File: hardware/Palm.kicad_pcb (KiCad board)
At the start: 2 copper layers, 29.8 x 70.5 mm, 13 parts, among them J1 Conn_01x02_Female, Q1 IRLML6402, SW1 SW_SPDT, SW2 SW_SPDT, U1 Adafruit_nRF52_Feather, U2 VEML6075_breakout

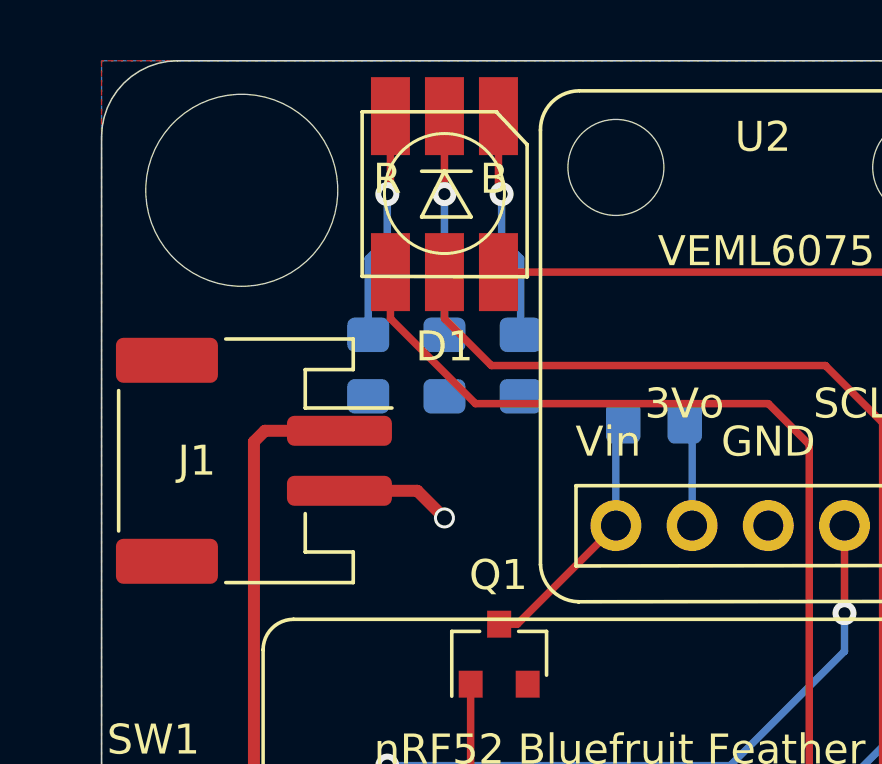
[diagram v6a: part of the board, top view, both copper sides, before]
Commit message: [footprint] Add more silkscreen annotations
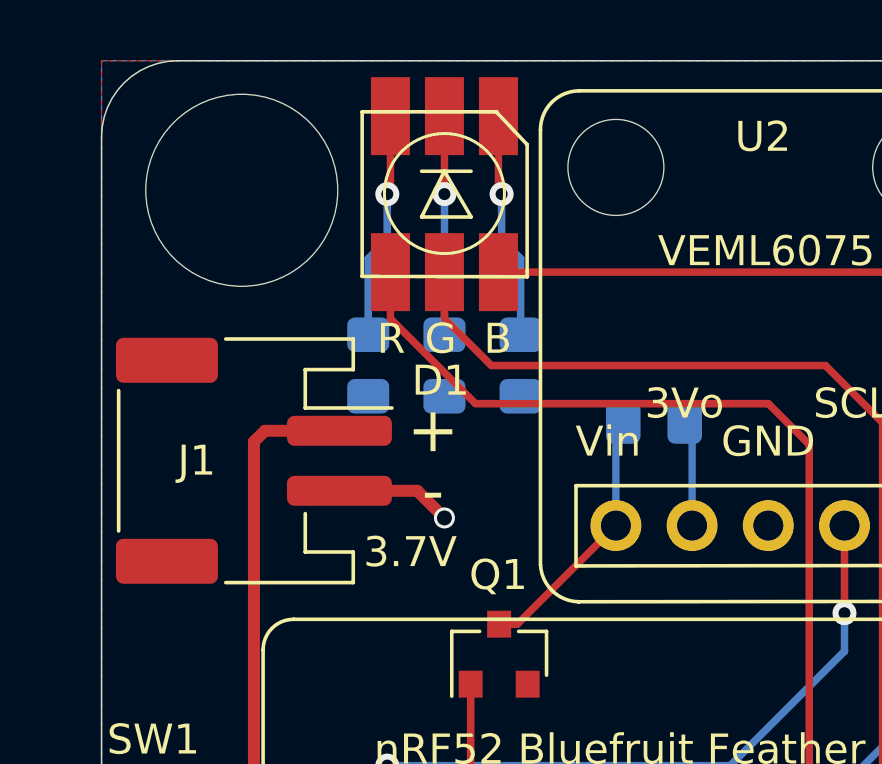
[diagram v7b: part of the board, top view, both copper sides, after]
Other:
- board text added: "+"
- board text added: "-"
- board text added: "3.7V"
- board text added: "G"
- board text added: "Option / DNP: Enable 4-pin sensor board"
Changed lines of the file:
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@@
   (general
     (thickness 1.6)
-    (drawings 14)
+    (drawings 19)
     (tracks 90)
     (zones 0)
@@
       (effects (font (size 1 1) (thickness 0.15)))
     )
-    (fp_text user VEML6075 (at -0.127 -3.175) (layer B.SilkS)
+    (fp_text user VEML6075 (at 0 -8.128) (layer B.SilkS)
       (effects (font (size 1 1) (thickness 0.15)) (justify mirror))
     )
@@
   (module CREE_RGB_LED_-PLCC-6_5.5x5.5mm:LED_RGB_Cree-PLCC-6_5.5x5.5mm_P2.1mm (layer F.Cu)
     (at 141.605 55.88 270)
-    (fp_text reference D1 (at 5.08 0) (layer F.SilkS)
+    (fp_text reference D1 (at 6.223 0.127) (layer F.SilkS)
       (effects (font (size 1 1) (thickness 0.15)))
     )
@@
       (effects (font (size 1 1) (thickness 0.15)))
     )
-    (fp_text user B (at -0.508 -1.651) (layer F.SilkS)
-      (effects (font (size 1 1) (thickness 0.15)))
-    )
-    (fp_text user R (at -0.508 1.905) (layer F.SilkS)
+    (fp_text user B (at 4.826 -1.778) (layer F.SilkS)
+      (effects (font (size 1 1) (thickness 0.15)))
+    )
+    (fp_text user R (at 4.826 1.778) (layer F.SilkS)
       (effects (font (size 1 1) (thickness 0.15)))
     )
@@
       (effects (font (size 1 1) (thickness 0.15)) (justify mirror))
     )
-    (fp_text value 0R (at 0 -1.65) (layer B.Fab)
+    (fp_text value 0R (at 0 1.651) (layer B.Fab)
       (effects (font (size 1 1) (thickness 0.15)) (justify mirror))
     )
@@
     )
   )
+  (gr_text 3.7V (at 140.462 67.818) (layer F.SilkS)
+    (effects (font (size 1 1) (thickness 0.15)))
+  )
+  (gr_text G (at 141.478 60.706) (layer F.SilkS)
+    (effects (font (size 1 1) (thickness 0.15)))
+  )
+  (gr_text "Option / DNP:\nEnable 4-pin\nsensor board" (at 156.464 59.944) (layer B.SilkS)
+    (effects (font (size 1 1) (thickness 0.15)) (justify left mirror))
+  )
+  (gr_text + (at 141.224 63.754) (layer F.SilkS)
+    (effects (font (size 1.5 1.5) (thickness 0.3)))
+  )
+  (gr_text - (at 141.224 65.786) (layer F.SilkS)
+    (effects (font (size 1.5 1.5) (thickness 0.3)))
+  )
   (gr_text "Get started at hutscape.com/palm" (at 144.145 88.9 270) (layer B.SilkS)
